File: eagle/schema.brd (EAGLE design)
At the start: 60.1 x 40.3 mm, 13 parts, among them IC1 LM1117T-3.3-V

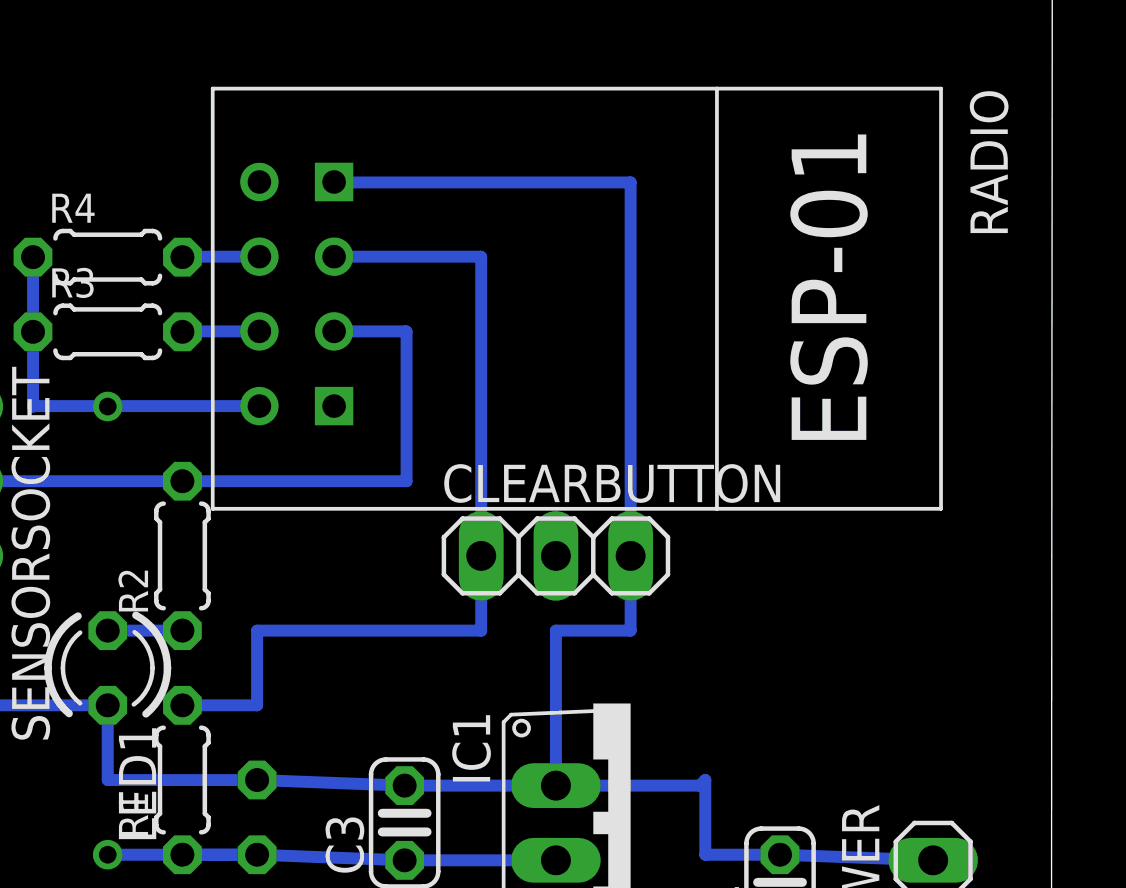
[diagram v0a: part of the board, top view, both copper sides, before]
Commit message: added light sensor
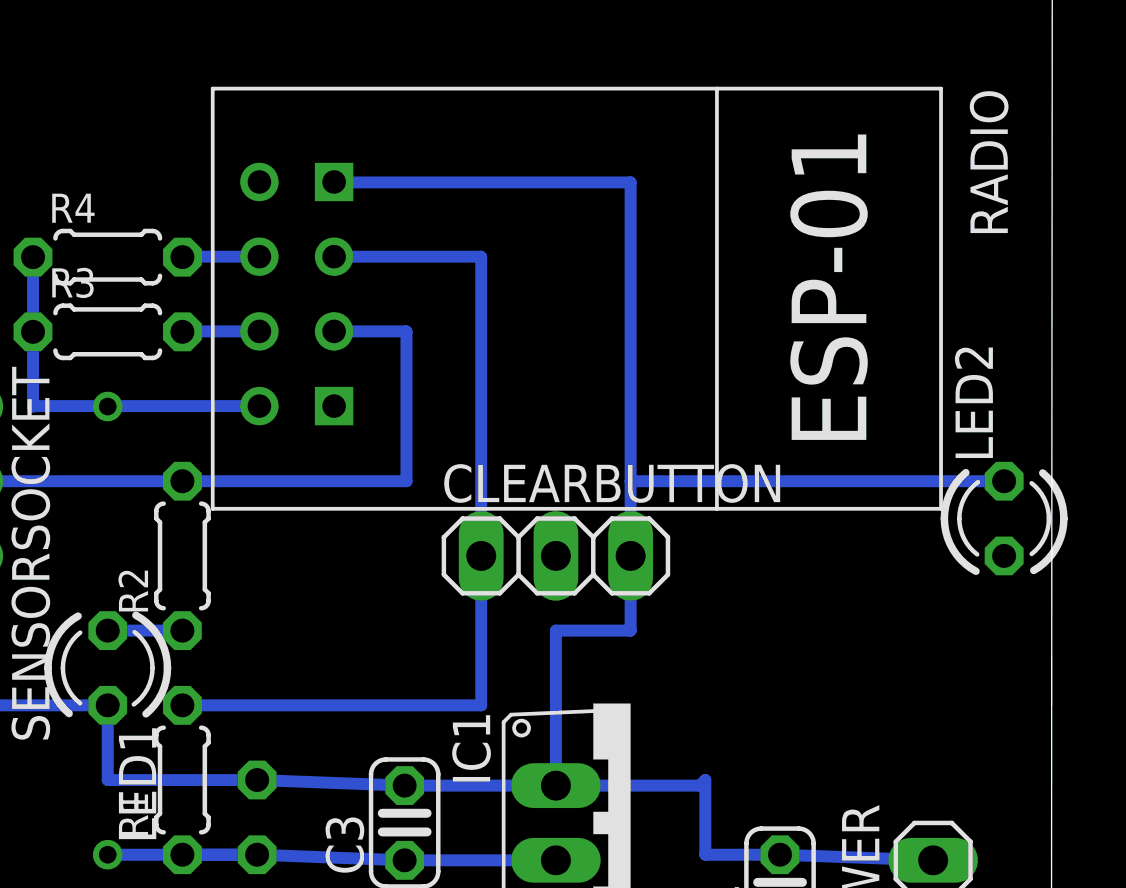
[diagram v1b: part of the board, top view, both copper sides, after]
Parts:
- added LED2: (no value), led:LED3MM
- R1: value 10k -> 47k
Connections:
- net CLEAR: now also LED2.A
- net GND: now also LED2.K
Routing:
- net GND: track 76.5 -> 89.2 mm
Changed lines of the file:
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@@
 <element name="LED1" library="led" package="LED3MM" value="" x="27.94" y="54.61" rot="R270"/>
 <element name="SENSORSOCKET" library="pinhead" package="1X03" value="" x="22.86" y="60.96" rot="R270"/>
-<element name="R1" library="rcl" package="0204/5" value="10k" x="30.48" y="50.8" rot="R90"/>
+<element name="R1" library="rcl" package="0204/5" value="47k" x="30.48" y="50.8" rot="R90"/>
 <element name="CLEARBUTTON" library="pinhead" package="1X03" value="" x="43.18" y="58.42"/>
+<element name="LED2" library="led" package="LED3MM" value="" x="58.42" y="59.69" rot="R90"/>
 </elements>
 <signals>
@@
 <wire x1="35.6375" y1="71.135" x2="35.6525" y2="71.12" width="0.4064" layer="16"/>
 <wire x1="35.6525" y1="71.12" x2="45.72" y2="71.12" width="0.4064" layer="16"/>
-<wire x1="45.72" y1="71.12" x2="45.72" y2="58.42" width="0.4064" layer="16"/>
+<wire x1="45.72" y1="71.12" x2="45.72" y2="60.96" width="0.4064" layer="16"/>
+<wire x1="45.72" y1="60.96" x2="45.72" y2="58.42" width="0.4064" layer="16"/>
 <wire x1="43.18" y1="50.6095" x2="43.18" y2="55.88" width="0.4064" layer="16"/>
 <wire x1="43.18" y1="55.88" x2="45.72" y2="55.88" width="0.4064" layer="16"/>
@@
 <wire x1="27.94" y1="53.34" x2="22.86" y2="53.34" width="0.4064" layer="16"/>
 <wire x1="22.86" y1="53.34" x2="22.86" y2="58.42" width="0.4064" layer="16"/>
+<contactref element="LED2" pad="K"/>
+<wire x1="58.42" y1="60.96" x2="45.72" y2="60.96" width="0.4064" layer="16"/>
 </signal>
 <signal name="+3V3">
@@
 <wire x1="25.415" y1="63.515" x2="33.0975" y2="63.515" width="0.4064" layer="16"/>
 <wire x1="33.02" y1="48.26" x2="27.94" y2="48.26" width="0.4064" layer="16"/>
-<wire x1="27.94" y1="48.26" x2="27.94" y2="63.515" width="0" layer="19" extent="1-16"/>
+<wire x1="33.02" y1="48.26" x2="33.0975" y2="63.515" width="0" layer="19" extent="1-1"/>
 </signal>
 <signal name="CHPD">
@@
 <contactref element="R1" pad="2"/>
 <contactref element="CLEARBUTTON" pad="1"/>
-<wire x1="40.64" y1="58.42" x2="40.64" y2="55.88" width="0.4064" layer="16"/>
-<wire x1="40.64" y1="55.88" x2="33.02" y2="55.88" width="0.4064" layer="16"/>
-<wire x1="33.02" y1="55.88" x2="33.02" y2="53.34" width="0.4064" layer="16"/>
-<wire x1="33.02" y1="53.34" x2="30.48" y2="53.34" width="0.4064" layer="16"/>
 <wire x1="40.64" y1="58.42" x2="40.64" y2="68.58" width="0.4064" layer="16"/>
 <wire x1="40.64" y1="68.58" x2="40.625" y2="68.595" width="0.4064" layer="16"/>
 <wire x1="40.625" y1="68.595" x2="35.6375" y2="68.595" width="0.4064" layer="16"/>
+<contactref element="LED2" pad="A"/>
+<wire x1="40.64" y1="58.42" x2="58.42" y2="58.42" width="0" layer="19" extent="1-1"/>
+<wire x1="30.48" y1="53.34" x2="40.64" y2="53.34" width="0.4064" layer="16"/>
+<wire x1="40.64" y1="53.34" x2="40.64" y2="58.42" width="0.4064" layer="16"/>
 </signal>
 <signal name="N$2">

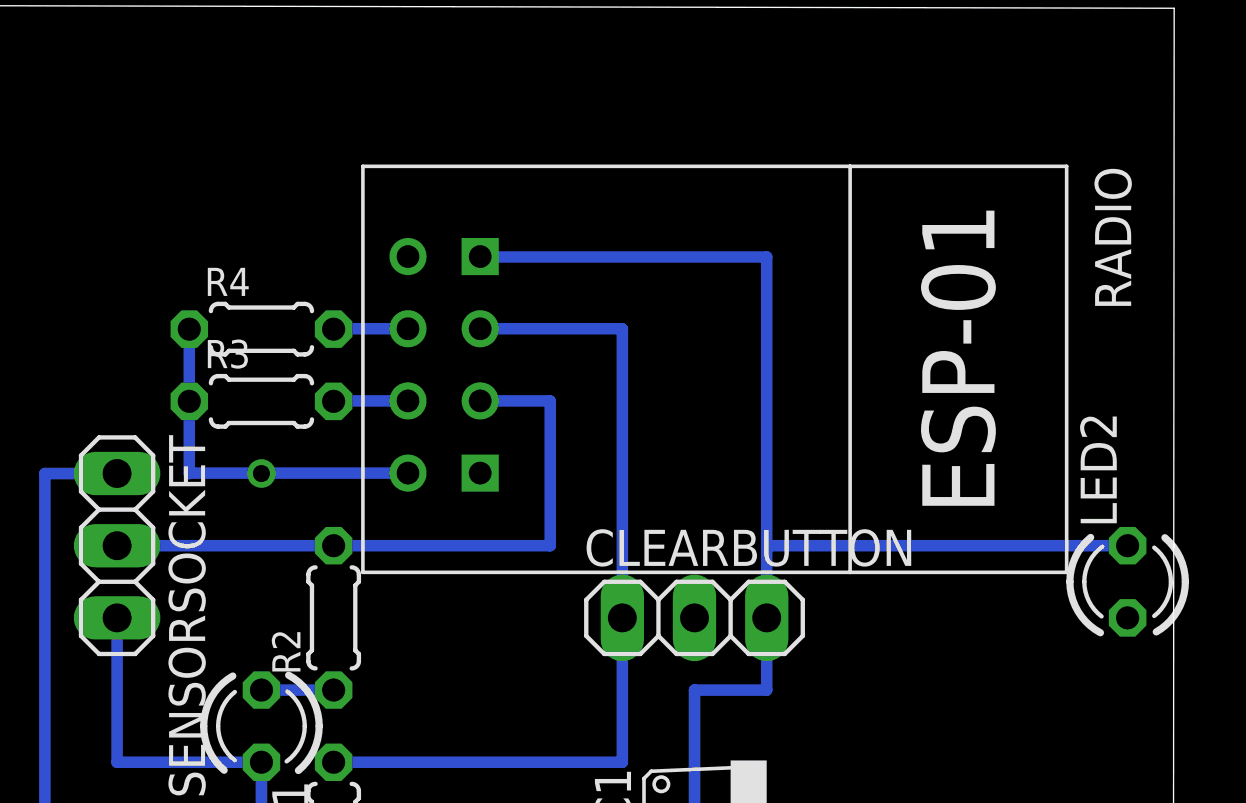
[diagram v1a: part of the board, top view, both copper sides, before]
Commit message: lights pin changed for well boot
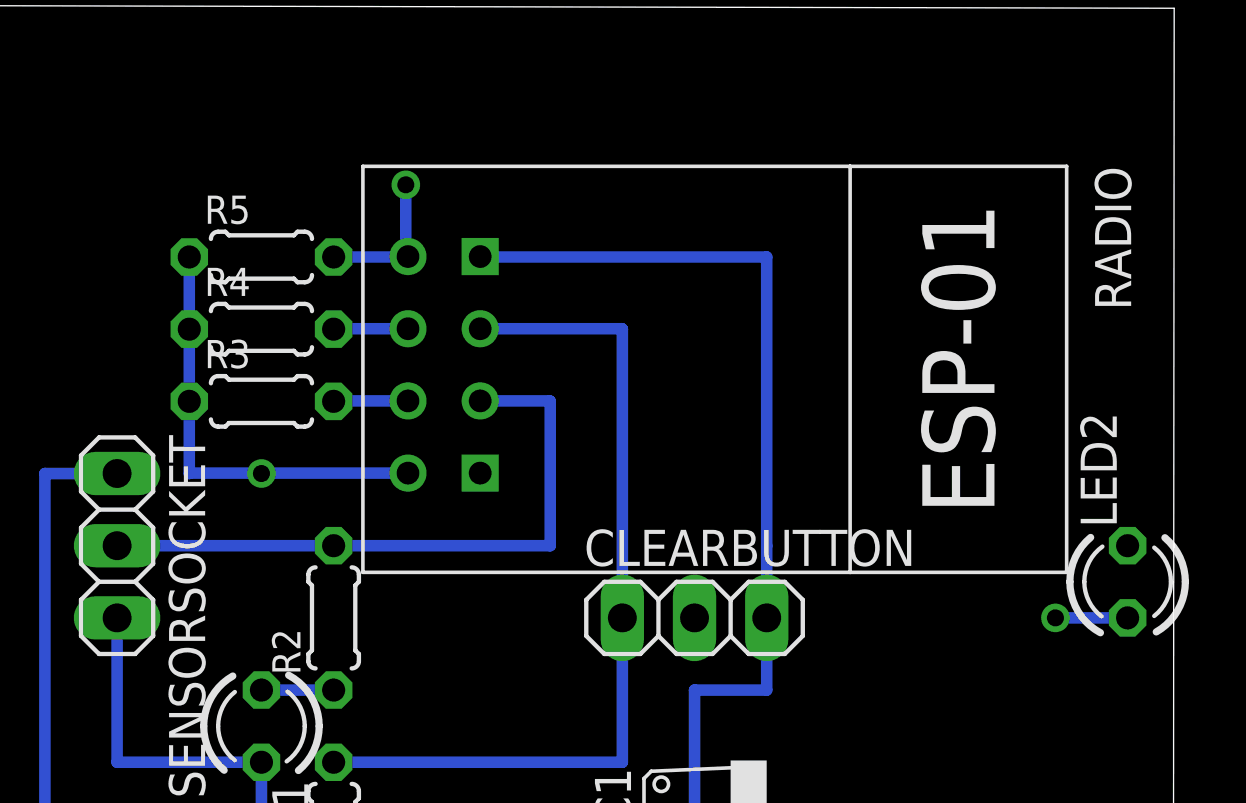
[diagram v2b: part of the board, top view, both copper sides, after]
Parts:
- added R5: 47k, rcl:0204/5
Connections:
- new net LIGHTS: LED2.A, R5.2, RADIO.TX
- net +3V3: now also R5.1
- net CLEAR: no longer LED2.A
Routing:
- net GND: track 89.2 -> 76.5 mm
- net LIGHTS: track 0.00 -> 7.77 mm
- net +3V3: track 30.6 -> 33.1 mm
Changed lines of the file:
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@@
 <element name="CLEARBUTTON" library="pinhead" package="1X03" value="" x="43.18" y="58.42"/>
 <element name="LED2" library="led" package="LED3MM" value="" x="58.42" y="59.69" rot="R90"/>
+<element name="R5" library="rcl" package="0204/5" value="47k" x="27.94" y="71.12"/>
 </elements>
 <signals>
@@
 <wire x1="22.86" y1="53.34" x2="22.86" y2="58.42" width="0.4064" layer="16"/>
 <contactref element="LED2" pad="K"/>
-<wire x1="58.42" y1="60.96" x2="45.72" y2="60.96" width="0.4064" layer="16"/>
+<wire x1="45.72" y1="60.96" x2="58.42" y2="60.96" width="0" layer="19" extent="16-16"/>
 </signal>
 <signal name="+3V3">
@@
 <wire x1="25.415" y1="63.515" x2="33.0975" y2="63.515" width="0.4064" layer="16"/>
 <wire x1="33.02" y1="48.26" x2="27.94" y2="48.26" width="0.4064" layer="16"/>
+<contactref element="R5" pad="1"/>
 <wire x1="33.02" y1="48.26" x2="33.0975" y2="63.515" width="0" layer="19" extent="1-1"/>
+<wire x1="25.4" y1="68.58" x2="25.4" y2="71.12" width="0.4064" layer="16"/>
 </signal>
 <signal name="CHPD">
@@
 <wire x1="40.64" y1="68.58" x2="40.625" y2="68.595" width="0.4064" layer="16"/>
 <wire x1="40.625" y1="68.595" x2="35.6375" y2="68.595" width="0.4064" layer="16"/>
-<contactref element="LED2" pad="A"/>
-<wire x1="40.64" y1="58.42" x2="58.42" y2="58.42" width="0" layer="19" extent="1-1"/>
 <wire x1="30.48" y1="53.34" x2="40.64" y2="53.34" width="0.4064" layer="16"/>
 <wire x1="40.64" y1="53.34" x2="40.64" y2="58.42" width="0.4064" layer="16"/>
@@
 <via x="27.94" y="48.26" extent="1-16" drill="0.6" shape="square"/>
 </signal>
+<signal name="LIGHTS">
+<contactref element="RADIO" pad="TX"/>
+<contactref element="R5" pad="2"/>
+<contactref element="LED2" pad="A"/>
+<wire x1="30.48" y1="71.12" x2="33.0975" y2="71.12" width="0.4064" layer="16"/>
+<wire x1="33.0975" y1="71.12" x2="33.0975" y2="71.135" width="0.4064" layer="16"/>
+<wire x1="33.0975" y1="71.135" x2="33.02" y2="71.135" width="0.4064" layer="16"/>
+<wire x1="33.02" y1="71.135" x2="33.02" y2="73.66" width="0.4064" layer="16"/>
+<wire x1="58.42" y1="58.42" x2="55.88" y2="58.42" width="0.4064" layer="16"/>
+<wire x1="33.0975" y1="71.12" x2="55.88" y2="58.42" width="0" layer="19" extent="16-16"/>
+</signal>
+<signal name="N$6">
+<via x="33.02" y="73.66" extent="1-16" drill="0.6" shape="square"/>
+</signal>
+<signal name="N$7">
+<via x="55.88" y="58.42" extent="1-16" drill="0.6" shape="square"/>
+</signal>
 </signals>
